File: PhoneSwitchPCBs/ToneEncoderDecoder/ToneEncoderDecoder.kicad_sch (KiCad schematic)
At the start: 142 parts

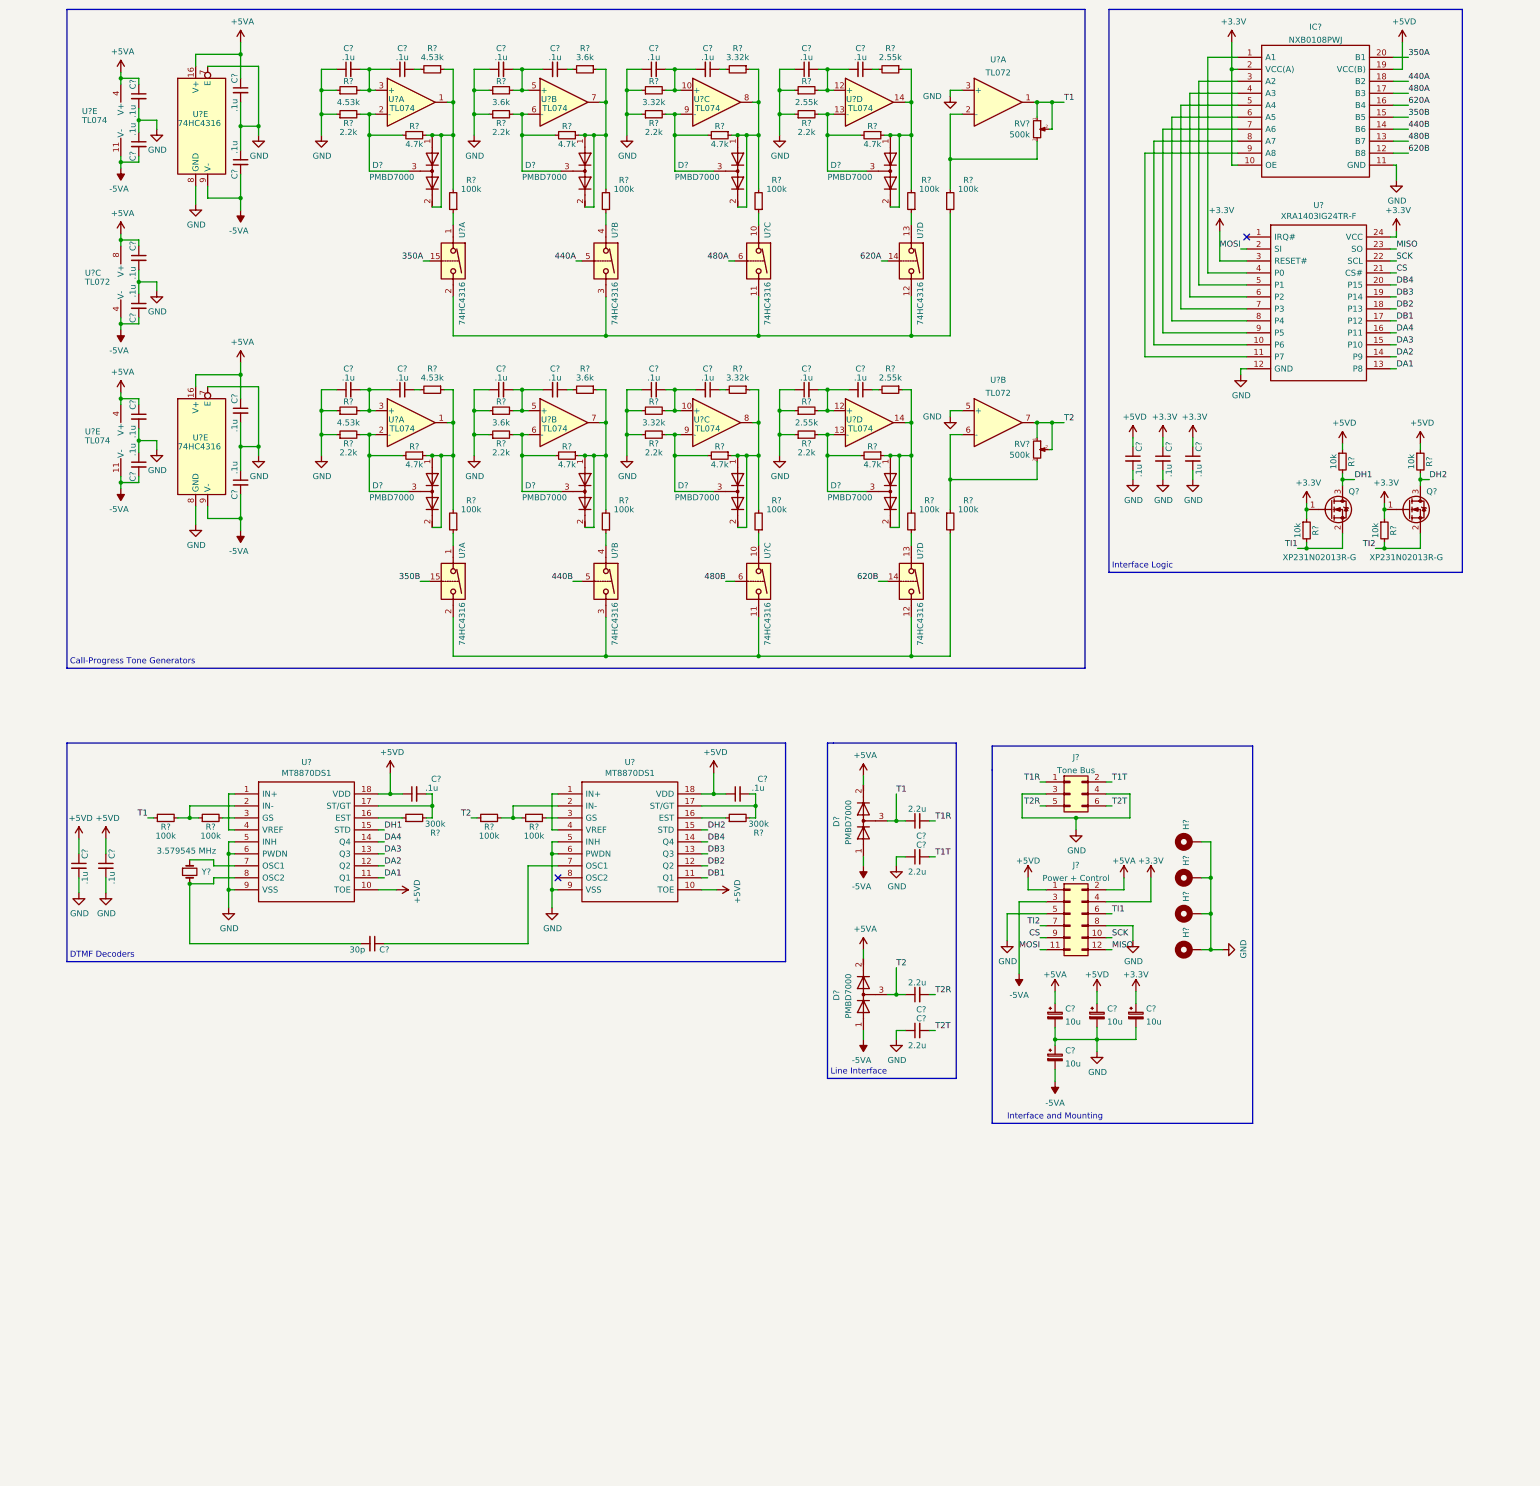
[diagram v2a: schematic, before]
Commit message: Finished schematic, started work on PCB design.
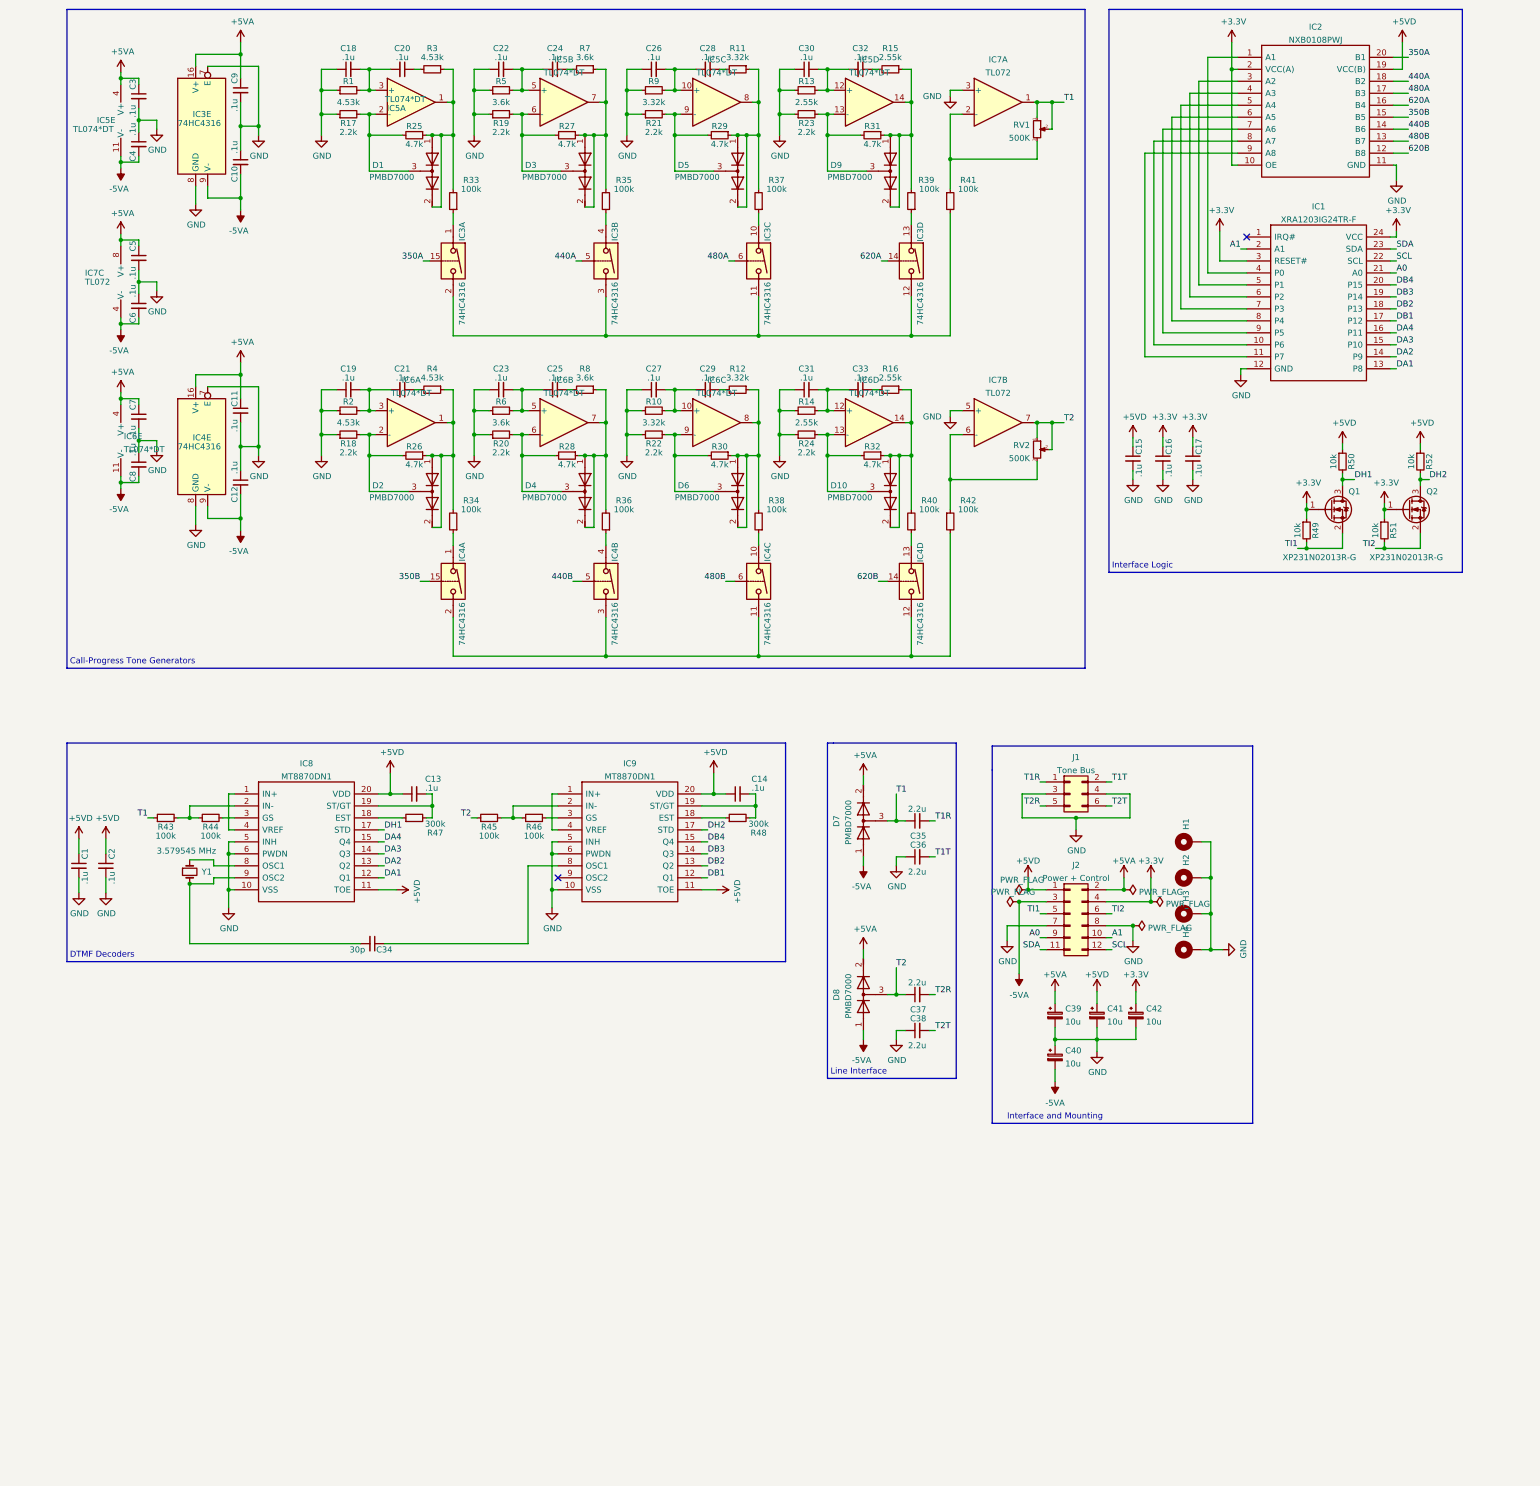
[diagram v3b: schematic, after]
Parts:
- removed C?: .1u, Capacitor_SMD:C_0603_1608Metric_Pad1.08x0.95mm_HandSolder, symbol Device:C_Small
- removed IC?: NXB0108PWJ, SOP65P640X110-20N, symbol SamacSys_Parts:NXB0108PWJ
- removed RV? (x2): 500k, Imported_Parts:TC33X-2_1, symbol Device:R_POT_Small
- removed U? (x10): TL074, Package_SO:SOIC-14_3.9x8.7mm_P1.27mm, symbol Amplifier_Operational:TL074
- removed U? (x2): MT8870DS1, Package_SO:SOIC-18W_7.5x11.6mm_P1.27mm, symbol Imported_Parts:MT8870DS1
- removed U?: XRA1403IG24TR-F, Package_SO:TSSOP-24_4.4x7.8mm_P0.65mm, symbol Imported_Parts:XRA1403IG24TR-F
- added C1: .1u, Capacitor_SMD:C_0603_1608Metric_Pad1.08x0.95mm_HandSolder, symbol Device:C_Small
- added IC1: XRA1203IG24TR-F, Package_SO:TSSOP-24_4.4x7.8mm_P0.65mm, symbol SwitchBackplaneParts:XRA1203IG24TR-F
- added IC2: NXB0108PWJ, Package_SO:TSSOP-20_4.4x6.5mm_P0.65mm, symbol SwitchBackplaneParts:NXB0108PWJ
- added IC5, IC6: TL074*DT, Package_SO:SOIC-14_3.9x8.7mm_P1.27mm, symbol SwitchBackplaneParts:TL074*DT
- added IC8, IC9: MT8870DN1, Package_SO:SSOP-20_5.3x7.2mm_P0.65mm, symbol SwitchBackplaneParts:MT8870DN1
- added RV1, RV2: 500K, Potentiometer_THT:Potentiometer_Bourns_3296W_Vertical, symbol Device:R_Potentiometer_Small
- C35, C36, C37, C38: renamed from C?; footprint Capacitor_THT:CP_Radial_D6.3mm_P2.50mm -> Capacitor_THT:C_Radial_D5.0mm_H11.0mm_P2.00mm
- C39, C40, C41, C42: renamed from C?; footprint (none) -> Capacitor_SMD:C_0805_2012Metric_Pad1.18x1.45mm_HandSolder
- H1, H2, H3, H4: renamed from H?; footprint (none) -> MountingHole:MountingHole_3.2mm_M3_Pad
- IC3, IC4: renamed from U?; footprint Package_SO:SO-16_3.9x9.9mm_P1.27mm -> Package_SO:TSSOP-16_4.4x5mm_P0.65mm
- IC7: renamed from U?; footprint (none) -> Package_SO:SOIC-8_3.9x4.9mm_P1.27mm
- J1: renamed from J?; footprint (none) -> Connector_PinHeader_2.54mm:PinHeader_2x03_P2.54mm_Vertical
- J2: renamed from J?; footprint (none) -> Connector_PinHeader_2.54mm:PinHeader_2x06_P2.54mm_Vertical
- R1, R10, R11, R12, R13, R14, R15, R16, R17, R18, R19, R2, R20, R21, R22, R23, R24, R25, R26, R27, R28, R29, R3, R30, R31, R32, R33, R34, R35, R36, R37, R38, R39, R4, R40, R41, R42, R43, R44, R45, R46, R47, R48, R49, R5, R50, R51, R52, R6, R7, R8, R9: renamed from R?; footprint Resistor_SMD:R_0805_2012Metric_Pad1.20x1.40mm_HandSolder -> Resistor_SMD:R_0603_1608Metric_Pad0.98x0.95mm_HandSolder
- gave numbers to parts that had none: 46
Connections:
- net +3V3: now also IC1.24 (VCC), IC1.3 (RESET#), IC2.10 (OE), IC2.2 (VCC(A))
- net +5VA: now also IC5.4 (V+), IC6.4 (V+)
- net +5VD: now also C1.1, IC2.19 (VCC(B)), IC8.11 (TOE), IC8.20 (VDD), IC9.11 (TOE), IC9.20 (VDD)
- net -5VA: now also IC5.11 (V-), IC6.11 (V-)
- net 350A: now also IC2.20 (B1)
- net 350B: now also IC2.15 (B5)
- net 440A: now also IC2.18 (B2)
- net 440B: now also IC2.14 (B6)
- net 480A: now also IC2.17 (B3)
- net 480B: now also IC2.13 (B7)
- net 620A: now also IC2.16 (B4)
- net 620B: now also IC2.12 (B8)
- net DA1: now also IC1.13 (P8), IC8.12 (Q1)
- net DA2: now also IC1.14 (P9), IC8.13 (Q2)
- net DA3: now also IC1.15 (P10), IC8.14 (Q3)
- net DA4: now also IC1.16 (P11), IC8.15 (Q4)
- net DB1: now also IC1.17 (P12), IC9.12 (Q1)
- net DB2: now also IC1.18 (P13), IC9.13 (Q2)
- net DB3: now also IC1.19 (P14), IC9.14 (Q3)
- net DB4: now also IC1.20 (P15), IC9.15 (Q4)
- net DH1: now also IC8.17 (STD)
- net DH2: now also IC9.17 (STD)
- net GND: now also J2.7 (Pin_7), C1.2, IC1.12 (GND), IC2.11 (GND), IC8.10 (VSS), IC8.5 (INH), IC8.6 (PWDN), IC9.10 (VSS), IC9.5 (INH), IC9.6 (PWDN); no longer J2.5 (Pin_5)
- net T1: now also RV1.1, RV1.2
- net T2: now also RV2.1, RV2.2
- net TI1: now also J2.5 (Pin_5); no longer J2.6 (Pin_6)
- net TI2: now also J2.6 (Pin_6); no longer J2.7 (Pin_7)
- net at C30.2, C32.2, R13.2: now also IC5.12 (+)
- net at C23.2, C25.2, R6.2: now also IC6.5 (+)
- net at D9.3 (K1A2), R23.2, R31.2: now also IC5.13 (-)
- net at D9.1 (A1), D9.2 (K2), R15.1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: now also IC5.14
- net at D1.1 (A1), D1.2 (K2), R25.1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: now also IC5.1
- net at D1.3 (K1A2), R17.2, R25.2: now also IC5.2 (-)
- net at C31.2, C33.2, R14.2: now also IC6.12 (+)
- net at D6.1 (A1), D6.2 (K2), R12.1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: now also IC6.8
- net at C22.2, C24.2, R5.2: now also IC5.5 (+)
- net at C18.2, C20.2, R1.2: now also IC5.3 (+)
- net at R48.1: now also IC9.18 (EST)
- net at C14.2, R48.2: now also IC9.19 (ST/GT)
- net at R45.2, R46.1: now also IC9.2 (IN-)
- net at R46.2: now also IC9.3 (GS)
- net at C34.1: now also IC9.8 (OSC1)
- net at D3.3 (K1A2), R19.2, R27.2: now also IC5.6 (-)
- net at D5.1 (A1), D5.2 (K2), R11.1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: now also IC5.8
- net at D4.1 (A1), D4.2 (K2), R28.1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: now also IC6.7
- net at R43.2, R44.1: now also IC8.2 (IN-)
- net at R44.2: now also IC8.3 (GS)
- net at R47.1: now also IC8.18 (EST)
- net at C13.2, R47.2: now also IC8.19 (ST/GT)
- net at C27.2, C29.2, R10.2: now also IC6.10 (+)
- net at D3.1 (A1), D3.2 (K2), R27.1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: now also IC5.7
- net at D10.1 (A1), D10.2 (K2), R16.1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: now also IC6.14
- net at C19.2, C21.2, R2.2: now also IC6.3 (+)
- net at C26.2, C28.2, R9.2: now also IC5.10 (+)
- net at D2.1 (A1), D2.2 (K2), R26.1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: now also IC6.1
- net at D2.3 (K1A2), R18.2, R26.2: now also IC6.2 (-)
- net at D10.3 (K1A2), R24.2, R32.2: now also IC6.13 (-)
- net at D6.3 (K1A2), R22.2, R30.2: now also IC6.9 (-)
- net at C34.2, Y1.2: now also IC8.9 (OSC2)
- net at D5.3 (K1A2), R21.2, R29.2: now also IC5.9 (-)
- net at IC7.6 (-), R42.1: now also RV2.3
- net at D4.3 (K1A2), R20.2, R28.2: now also IC6.6 (-)
- net at IC7.2 (-), R41.1: now also RV1.3
- net at Y1.1: now also IC8.8 (OSC1)
- net CS renamed A0
- net A0: now also IC1.21 (A0)
- net MISO renamed SCL
- net SCL: now also IC1.22 (SCL)
- net MOSI renamed SDA
- net SDA: now also IC1.23 (SDA)
- net SCK renamed A1
- net A1: now also IC1.2 (A1)
- new net: IC8.1 (IN+), IC8.4 (VREF)
- new net: IC9.1 (IN+), IC9.4 (VREF)
- new net: IC1.4 (P0), IC2.1 (A1)
- new net: IC1.5 (P1), IC2.3 (A2)
- new net: IC1.6 (P2), IC2.4 (A3)
- new net: IC1.7 (P3), IC2.5 (A4)
- new net: IC1.8 (P4), IC2.6 (A5)
- new net: IC1.9 (P5), IC2.7 (A6)
- new net: IC1.10 (P6), IC2.8 (A7)
- new net: IC1.11 (P7), IC2.9 (A8)
